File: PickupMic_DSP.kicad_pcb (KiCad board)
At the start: 4 copper layers, 70 x 59.8 mm, 46 parts, among them J201 Barrel_Jack, J301 Piezos, J401 USB_B_Micro, J402 SWD, U201 AMS1117-3.3, U202 AMS1117-5.0, U203 AMS1117-3.3, U301 TL082, U302 TL082, U303 ADS1115IDGS, U401 USBLC6-2SC6, U402 STM32F405RGTx, Y401 25Mhz

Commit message: Switch ADC
Switched from the ADS1115 to ADS7924 to get faster sampling time.
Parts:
- added C305: 1u, Capacitor_SMD:C_0402_1005Metric, F.Cu at (98.2, 93.8)
- added C306: 1u, Capacitor_SMD:C_0402_1005Metric, F.Cu at (98.2, 96.0)
- added D202: RED, LED_SMD:LED_0805_2012Metric, F.Cu at (100.0, 66.0)
- added D402: GREEN, LED_SMD:LED_0805_2012Metric, F.Cu at (103.4, 80.0)
- added kibuzzard-63BB1A01: G***, kibuzzard-63BB1A01, F.Cu at (124.2, 115.0)
- added kibuzzard-63BB1A56: G***, kibuzzard-63BB1A56, F.Cu at (124.2, 117.6)
- added kibuzzard-63BB1A7D: G***, kibuzzard-63BB1A7D, F.Cu at (124.4, 110.0)
- added kibuzzard-63BB1AB4: G***, kibuzzard-63BB1AB4, F.Cu at (135.0, 107.0)
- added kibuzzard-63BB1BAF: G***, kibuzzard-63BB1BAF, F.Cu at (100.2, 71.5)
- added kibuzzard-63C77ADE: G***, kibuzzard-63C77ADE, F.Cu at (77.8, 66.8)
- added kibuzzard-63C77B3E: G***, kibuzzard-63C77B3E, F.Cu at (101.4, 77.6)
- added kibuzzard-63CD6EAA: G***, kibuzzard-63CD6EAA, F.Cu at (124.2, 112.6)
- D201: value RED -> SS54; footprint LED_SMD:LED_0805_2012Metric -> Diode_SMD:D_SMA
- D401: value GREEN -> SS54; footprint LED_SMD:LED_0805_2012Metric -> Diode_SMD:D_SMA
- U303: value ADS1115IDGS -> ADS7924; footprint Package_SO:TSSOP-10_3x3mm_P0.5mm -> Package_DFN_QFN:WQFN-16-1EP_3x3mm_P0.5mm_EP1.68x1.68mm
- moved R308 21.4 mm to (84.3, 104.7), turned to 90 degrees
- moved R305 21.2 mm to (105.7, 106.0), turned to 90 degrees
- moved D201 12.4 mm to (90.2, 74.6), turned to 180 degrees
- moved U302 12.2 mm to (88.8, 105.8), turned to 180 degrees
- moved U301 12.1 mm to (101.1, 105.8), turned to 180 degrees
- moved C301 7.63 mm to (131.8, 110.0)
- moved R301 7.63 mm to (128.4, 110.0)
- moved C304 7.60 mm to (131.8, 117.6)
- moved R304 7.60 mm to (128.5, 117.6)
- moved D401 5.69 mm to (102.8, 74.4)
- moved R306 3.71 mm to (96.5, 104.7), turned to 90 degrees
- moved R307 3.08 mm to (93.4, 106.0), turned to 90 degrees
- moved C303 2.55 mm to (131.8, 115.1)
- moved R303 2.55 mm to (128.5, 115.1)
- moved C302 2.49 mm to (131.8, 112.5)
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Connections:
- C201 pad 2: +12V -> Vin
- C202 pad 2: +12V -> Vin
- D201 pad 1: Net-(D201-Pad1) -> Vin
- D201 pad 2: +3.3V -> Net-(D201-Pad2)
- D401 pad 1: Net-(D401-Pad1) -> Vin
- D401 pad 2: /Microcontroller/MCU_LED -> VBUS
- J201 pad 1: +12V -> Net-(D201-Pad2)
- J301 pad 2: /Analog In/AIN3 -> /Analog In/AIN0
- J301 pad 4: /Analog In/AIN2 -> /Analog In/AIN1
- J301 pad 6: /Analog In/AIN1 -> /Analog In/AIN2
- J301 pad 8: /Analog In/AIN0 -> /Analog In/AIN3
- R201 pad 1: Net-(D201-Pad1) -> Net-(D202-Pad1)
- R401 pad 1: Net-(D401-Pad1) -> Net-(D402-Pad1)
- U201 pad 3: +12V -> Vin
- U202 pad 3: +12V -> Vin
- U303 pad 1: GND -> unconnected-(U303-Pad1)
- U303 pad 10: /Analog In/MCU_SCL -> /Analog In/ADC_AIN2
- U303 pad 3: GND -> /Analog In/MCU_SCL
- U303 pad 4: /Analog In/ADC_AIN0 -> /Analog In/MCU_SDA
- U303 pad 5: /Analog In/ADC_AIN1 -> GND
- U303 pad 6: /Analog In/ADC_AIN2 -> GND
- U303 pad 7: /Analog In/ADC_AIN3 -> unconnected-(U303-Pad7)
- U303 pad 8: +5VA -> GND
- U303 pad 9: /Analog In/MCU_SDA -> /Analog In/ADC_AIN3
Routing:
- net Vin: track 0.00 -> 42.0 mm
- net /Analog In/FILT_AIN3: track 24.9 -> 60.4 mm
- net +12V: track 33.0 -> 0.00 mm
- net /Analog In/FILT_AIN0: track 53.8 -> 26.1 mm
- net VBUS: track 6.97 -> 21.7 mm, vias 0 -> 2
- net +3.3V: track 36.8 -> 28.1 mm, vias 16 -> 41
- net +5VA: track 59.8 -> 67.3 mm
- net /Analog In/ADC_AIN2: track 9.26 -> 15.0 mm
- net /Analog In/FILT_AIN2: track 39.2 -> 44.9 mm
- net Net-(D201-Pad2): track 0.00 -> 4.79 mm
- net GND: track 132.4 -> 128.7 mm, vias 53 -> 69
- net /Analog In/MCU_SDA: track 17.7 -> 21.0 mm, vias 0 -> 2
- net Net-(D202-Pad1): track 0.00 -> 3.19 mm
- net MCU_ADC_INT: track 22.5 -> 19.6 mm
- net /Analog In/ADC_AIN0: track 12.7 -> 15.2 mm
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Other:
- board text removed: "AIN0"
- board text removed: "AIN1"
- board text removed: "AIN2"
- board text removed: "AIN3"
- board text removed: "Blinky!"
- board text removed: "GND"
- board text removed: "Power"
- board text removed: "VIN: 9-12V DC"

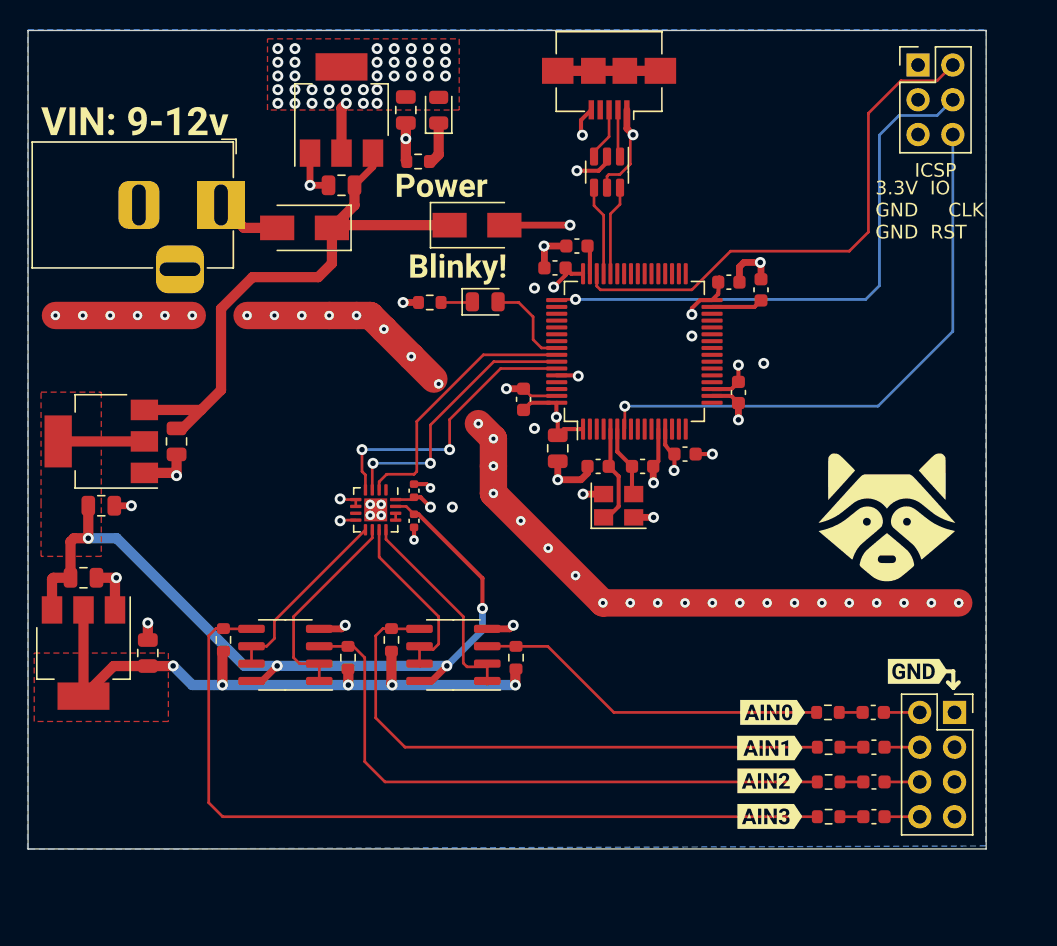
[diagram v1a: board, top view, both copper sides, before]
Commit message: Improvements
Switched ADC to ADC128S.
Upgraded USB to USB-C
Improved Analog front end to work with signals better.
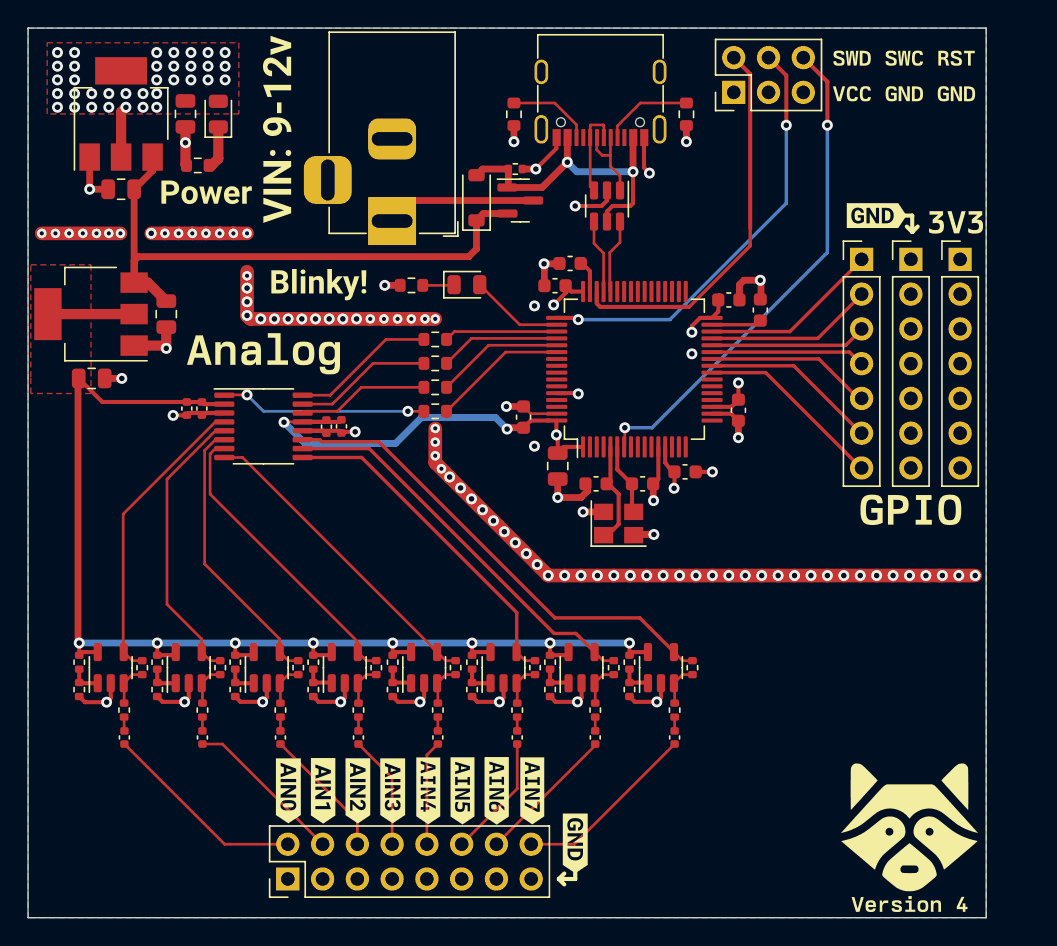
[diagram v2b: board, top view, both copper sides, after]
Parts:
- removed C205, C206: 22u, Capacitor_SMD:C_0805_2012Metric
- removed D401: SS54, Diode_SMD:D_SMA
- removed J402: SWD, Connector_PinHeader_2.54mm:PinHeader_2x03_P2.54mm_Vertical
- removed U203: AMS1117-3.3, Package_TO_SOT_SMD:SOT-223-3_TabPin2
- added C307: 1u, Capacitor_SMD:C_0402_1005Metric, F.Cu at (105.7, 111.8)
- added C308: 1u, Capacitor_SMD:C_0402_1005Metric, F.Cu at (99.9, 111.8)
- added C309: 1u, Capacitor_SMD:C_0402_1005Metric, F.Cu at (81.6, 87.8)
- added C310: 1u, Capacitor_SMD:C_0402_1005Metric, F.Cu at (92.9, 89.1)
- added C311: 100n, Capacitor_SMD:C_0402_1005Metric, F.Cu at (91.8, 89.1)
- added C312: 100n, Capacitor_SMD:C_0402_1005Metric, F.Cu at (82.7, 87.8)
- added J501: GPIO, Connector_PinHeader_2.54mm:PinHeader_1x07_P2.54mm_Vertical, F.Cu at (130.9, 76.9)
- added J502: VCC, Connector_PinHeader_2.54mm:PinHeader_1x07_P2.54mm_Vertical, F.Cu at (138.1, 76.9)
- added J503: GND, Connector_PinHeader_2.54mm:PinHeader_1x07_P2.54mm_Vertical, F.Cu at (134.5, 76.9)
- added J504: SWD, Connector_PinHeader_2.54mm:PinHeader_2x03_P2.54mm_Vertical, F.Cu at (121.6, 64.7)
- added Q201: AO3401A, Package_TO_SOT_SMD:SOT-23, F.Cu at (106.0, 72.6)
- added R202: 100k, Resistor_SMD:R_0402_1005Metric, F.Cu at (105.6, 70.3)
- added R309: 510R, Resistor_SMD:R_0402_1005Metric, F.Cu at (94.1, 109.8)
- added R310: 510R, Resistor_SMD:R_0402_1005Metric, F.Cu at (88.4, 109.8)
- added R311: 510R, Resistor_SMD:R_0402_1005Metric, F.Cu at (82.7, 109.8)
- added R312: 510R, Resistor_SMD:R_0402_1005Metric, F.Cu at (77.0, 109.8)
- added R313: 100k, Resistor_SMD:R_0402_1005Metric, F.Cu at (95.4, 106.7)
- added R314: 100k, Resistor_SMD:R_0402_1005Metric, F.Cu at (89.7, 106.7)
- added R315: 100k, Resistor_SMD:R_0402_1005Metric, F.Cu at (84.0, 106.7)
- added R316: 100k, Resistor_SMD:R_0402_1005Metric, F.Cu at (78.3, 106.7)
- added R317: 10k, Resistor_SMD:R_0402_1005Metric, F.Cu at (113.9, 106.3)
- added R318: 10k, Resistor_SMD:R_0402_1005Metric, F.Cu at (113.9, 108.3)
- added R319: 10k, Resistor_SMD:R_0402_1005Metric, F.Cu at (108.1, 106.3)
- added R320: 10k, Resistor_SMD:R_0402_1005Metric, F.Cu at (108.1, 108.3)
- added R321: 10k, Resistor_SMD:R_0402_1005Metric, F.Cu at (102.4, 106.3)
- added R322: 10k, Resistor_SMD:R_0402_1005Metric, F.Cu at (102.4, 108.3)
- added R323: 10k, Resistor_SMD:R_0402_1005Metric, F.Cu at (96.6, 106.3)
- added R324: 10k, Resistor_SMD:R_0402_1005Metric, F.Cu at (96.6, 108.3)
- added R325: 510R, Resistor_SMD:R_0402_1005Metric, F.Cu at (117.2, 109.8)
- added R326: 510R, Resistor_SMD:R_0402_1005Metric, F.Cu at (111.4, 109.8)
- added R327: 510R, Resistor_SMD:R_0402_1005Metric, F.Cu at (105.7, 109.8)
- added R328: 510R, Resistor_SMD:R_0402_1005Metric, F.Cu at (99.9, 109.8)
- added R329: 100k, Resistor_SMD:R_0402_1005Metric, F.Cu at (118.5, 106.7)
- added R330: 100k, Resistor_SMD:R_0402_1005Metric, F.Cu at (112.8, 106.7)
- added R331: 100k, Resistor_SMD:R_0402_1005Metric, F.Cu at (107.0, 106.7)
- added R332: 100k, Resistor_SMD:R_0402_1005Metric, F.Cu at (101.2, 106.7)
- added R402: 5.1k, Resistor_SMD:R_0603_1608Metric, F.Cu at (118.1, 66.3)
- added R403: 5.1k, Resistor_SMD:R_0603_1608Metric, F.Cu at (105.5, 66.3)
- added R404: 100, Resistor_SMD:R_0603_1608Metric, F.Cu at (99.8, 82.8)
- added R405: 100, Resistor_SMD:R_0603_1608Metric, F.Cu at (99.8, 84.5)
- added R406: 100, Resistor_SMD:R_0603_1608Metric, F.Cu at (99.8, 86.2)
- added R407: 100, Resistor_SMD:R_0603_1608Metric, F.Cu at (99.8, 88.0)
- added U304: LMV321, Package_TO_SOT_SMD:SOT-23-5, F.Cu at (76.0, 106.7)
- added U305: LMV321, Package_TO_SOT_SMD:SOT-23-5, F.Cu at (116.2, 106.7)
- added U306: LMV321, Package_TO_SOT_SMD:SOT-23-5, F.Cu at (110.4, 106.7)
- added U307: LMV321, Package_TO_SOT_SMD:SOT-23-5, F.Cu at (104.7, 106.7)
- added U308: LMV321, Package_TO_SOT_SMD:SOT-23-5, F.Cu at (98.9, 106.7)
- added U309: ADC128S102, Package_SO:TSSOP-16_4.4x5mm_P0.65mm, F.Cu at (87.2, 89.1)
- added kibuzzard-63BB1AB4: G***, kibuzzard-63BB1AB4, F.Cu at (132.0, 73.7)
- added kibuzzard-641D0A5C: G***, kibuzzard-641D0A5C, F.Cu at (101.7, 115.7)
- added kibuzzard-641D0A72: G***, kibuzzard-641D0A72, F.Cu at (104.2, 115.7)
- added kibuzzard-641D0A85: G***, kibuzzard-641D0A85, F.Cu at (106.8, 115.7)
- added kibuzzard-641E03D9: G***, kibuzzard-641E03D9, F.Cu at (99.2, 115.7)
- added kibuzzard-6422FB8B: G***, kibuzzard-6422FB8B, F.Cu at (137.8, 74.2)
- added kibuzzard-6422FF5E: G***, kibuzzard-6422FF5E, F.Cu at (134.4, 124.0)
- added kibuzzard-642304B8: G***, kibuzzard-642304B8, F.Cu at (134.5, 95.2)
- added kibuzzard-6423A336: G***, kibuzzard-6423A336, F.Cu at (87.2, 83.8)
- added kibuzzard-6423A404: G***, kibuzzard-6423A404, F.Cu at (134.0, 64.8)
- added kibuzzard-6423A41B: G***, kibuzzard-6423A41B, F.Cu at (134.0, 62.2)
- C301, C302, C303, C304: value 10u -> 1u; footprint Capacitor_SMD:C_0603_1608Metric -> Capacitor_SMD:C_0402_1005Metric
- C401: value 30p -> 2.2u
- C404: value 2.2u -> 30p
- D201: value SS54 -> MBR120; footprint Diode_SMD:D_SMA -> Diode_SMD:D_SOD-123
- J301: value Piezos -> AIN; footprint Connector_PinSocket_2.54mm:PinSocket_2x04_P2.54mm_Vertical -> Connector_PinHeader_2.54mm:PinHeader_2x08_P2.54mm_Vertical
- J401: value USB_B_Micro -> USB_C_Receptacle_USB2.0; footprint Connector_USB:USB_Micro-B_Amphenol_10104110_Horizontal -> Connector_USB:USB_C_Receptacle_G-Switch_GT-USB-7010ASV
- R301, R302, R303, R304, R305, R306, R307, R308: footprint Resistor_SMD:R_0603_1608Metric -> Resistor_SMD:R_0402_1005Metric
- U301, U302: value TL082 -> LMV321; footprint Package_SO:SOIC-8_3.9x4.9mm_P1.27mm -> Package_TO_SOT_SMD:SOT-23-5
- U303: value ADS7924 -> LMV321; footprint Package_DFN_QFN:WQFN-16-1EP_3x3mm_P0.5mm_EP1.68x1.68mm -> Package_TO_SOT_SMD:SOT-23-5
- Y401: value 25Mhz -> 16Mhz
- moved C304 55.1 mm to (77.0, 111.8), turned to 90 degrees
- moved J301 50.2 mm to (89.0, 122.2), turned to 90 degrees
- moved C303 49.2 mm to (82.7, 111.8), turned to 90 degrees
- moved R304 44.3 mm to (85.1, 108.3), turned to -90 degrees
- moved R303 44.2 mm to (85.1, 106.3), turned to -90 degrees
- moved C302 43.4 mm to (88.4, 111.8), turned to 90 degrees
- moved R302 37.9 mm to (90.8, 108.3), turned to 90 degrees
- moved R301 37.8 mm to (90.8, 106.3), turned to -90 degrees
- moved C301 37.7 mm to (94.1, 111.8), turned to 90 degrees
- moved kibuzzard-63BB1A7D 35.8 mm to (89.0, 115.7), turned to -90 degrees
- moved kibuzzard-63CD6EAA 32.8 mm to (91.6, 115.7), turned to -90 degrees
- moved kibuzzard-63BB1A01 30.1 mm to (94.1, 115.7), turned to -90 degrees
- moved kibuzzard-63BB1AB4 28.0 mm to (110.0, 119.6), turned to -90 degrees
- moved kibuzzard-63BB1A56 27.6 mm to (96.6, 115.7), turned to -90 degrees
- moved C305 26.2 mm to (117.2, 111.8)
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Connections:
- C201 pad 2: Vin -> +5V
- C202 pad 2: Vin -> +5V
- C301 pad 1: /Analog In/AIN0 -> /Analog In/AIN3
- C302 pad 1: /Analog In/AIN1 -> /Analog In/AIN2
- C303 pad 1: /Analog In/AIN2 -> /Analog In/AIN1
- C304 pad 1: /Analog In/AIN3 -> /Analog In/AIN0
- C305 pad 1: +3.3V -> /Analog In/AIN7
- C305 pad 2: GND -> Net-(C305-Pad2)
- C306 pad 1: +5VA -> /Analog In/AIN6
- C306 pad 2: GND -> Net-(C306-Pad2)
- C401 pad 1: /Microcontroller/MCU_PH0 -> /Microcontroller/MCU_VCAP1
- C402 pad 1: /Microcontroller/MCU_PH1 -> /Microcontroller/MCU_PH0
- C403 pad 1: /Microcontroller/MCU_VCAP1 -> /Microcontroller/MCU_VCAP2
- C404 pad 1: /Microcontroller/MCU_VCAP2 -> /Microcontroller/MCU_PH1
- D201 pad 1: Vin -> +5V
- D201 pad 2: Net-(D201-Pad2) -> VBUS
- J201 pad 1: Net-(D201-Pad2) -> Vin
- R301 pad 1: Net-(C301-Pad2) -> +5VA
- R301 pad 2: /Analog In/FILT_AIN0 -> Net-(U301-+)
- R302 pad 1: Net-(C302-Pad2) -> GND
- R302 pad 2: /Analog In/FILT_AIN1 -> Net-(U301-+)
- R303 pad 1: Net-(C303-Pad2) -> +5VA
- R303 pad 2: /Analog In/FILT_AIN2 -> Net-(U302-+)
- R304 pad 1: Net-(C304-Pad2) -> Net-(U302-+)
- R304 pad 2: /Analog In/FILT_AIN3 -> GND
- R305 pad 1: +3.3VA -> +5VA
- R305 pad 2: /Analog In/FILT_AIN0 -> Net-(U303-+)
- R306 pad 1: +3.3VA -> GND
- R306 pad 2: /Analog In/FILT_AIN1 -> Net-(U303-+)
- R307 pad 1: +3.3VA -> +5VA
- R307 pad 2: /Analog In/FILT_AIN2 -> Net-(U304-+)
- R308 pad 1: +3.3VA -> GND
- R308 pad 2: /Analog In/FILT_AIN3 -> Net-(U304-+)
- U201 pad 3: Vin -> +5V
- U202 pad 3: Vin -> +5V
- U301 pad 1: /Analog In/ADC_AIN0 -> Net-(U301-+)
- U301 pad 2: /Analog In/ADC_AIN0 -> GND
- U301 pad 3: /Analog In/FILT_AIN0 -> Net-(U301--)
- U301 pad 4: GND -> /Analog In/ADC_AIN3
- U301 pad 5: /Analog In/FILT_AIN1 -> +5VA
- U302 pad 1: /Analog In/ADC_AIN2 -> Net-(U302-+)
- U302 pad 2: /Analog In/ADC_AIN2 -> GND
- U302 pad 3: /Analog In/FILT_AIN2 -> Net-(U302--)
- U302 pad 4: GND -> /Analog In/ADC_AIN2
- U302 pad 5: /Analog In/FILT_AIN3 -> +5VA
- U303 pad 1: unconnected-(U303-Pad1) -> Net-(U303-+)
- U303 pad 2: MCU_ADC_INT -> GND
- U303 pad 3: /Analog In/MCU_SCL -> Net-(U303--)
- U303 pad 4: /Analog In/MCU_SDA -> /Analog In/ADC_AIN1
- U303 pad 5: GND -> +5VA
- U402 pad 24: unconnected-(U402-Pad24) -> MCU_GPIO_PC04
- U402 pad 25: unconnected-(U402-Pad25) -> MCU_GPIO_PC05
- U402 pad 26: unconnected-(U402-Pad26) -> MCU_GPIO_PB00
- U402 pad 27: unconnected-(U402-Pad27) -> MCU_GPIO_PB01
- U402 pad 28: unconnected-(U402-Pad28) -> MCU_GPIO_PB02
- U402 pad 29: unconnected-(U402-Pad29) -> MCU_GPIO_PB10
- U402 pad 30: unconnected-(U402-Pad30) -> MCU_GPIO_PB11
- U402 pad 46: /Microcontroller/MCU_SWD_IO -> MCU_SWD_IO
- U402 pad 49: /Microcontroller/MCU_SWD_CLK -> MCU_SWD_CLK
- U402 pad 50: unconnected-(U402-Pad50) -> /Microcontroller/MCU_LED
- U402 pad 51: unconnected-(U402-Pad51) -> Net-(U402-PC10)
- U402 pad 52: unconnected-(U402-Pad52) -> Net-(U402-PC11)
- U402 pad 53: unconnected-(U402-Pad53) -> Net-(U402-PC12)
- U402 pad 54: unconnected-(U402-Pad54) -> Net-(U402-PD2)
- U402 pad 56: /Microcontroller/MCU_LED -> unconnected-(U402-PB4-Pad56)
- U402 pad 57: MCU_ADC_INT -> unconnected-(U402-PB5-Pad57)
- U402 pad 58: /Analog In/MCU_SCL -> unconnected-(U402-PB6-Pad58)
- U402 pad 59: /Analog In/MCU_SDA -> unconnected-(U402-PB7-Pad59)
- U402 pad 7: /Microcontroller/MCU_NRST -> MCU_NRST
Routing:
- net /Analog In/FILT_AIN3: track 60.4 -> 0.00 mm
- net +3.3VA: track 46.5 -> 0.00 mm, vias 5 -> 0
- net /Analog In/FILT_AIN2: track 44.9 -> 0.00 mm
- net +5V: track 0.00 -> 44.2 mm
- net /Analog In/FILT_AIN1: track 42.6 -> 0.00 mm
- net /Microcontroller/MCU_NRST: track 42.3 -> 0.00 mm, vias 1 -> 0
- net /Microcontroller/MCU_SWD_CLK: track 41.4 -> 0.00 mm, vias 1 -> 0
- net GND: track 128.7 -> 168.3 mm, vias 69 -> 106
- net /Microcontroller/MCU_SWD_IO: track 38.9 -> 0.00 mm
- net MCU_NRST: track 0.00 -> 36.4 mm, vias 0 -> 2
- net /Analog In/ADC_AIN7: track 0.00 -> 35.2 mm
- net Vin: track 42.0 -> 8.80 mm
- net MCU_SWD_CLK: track 0.00 -> 31.5 mm, vias 0 -> 2
- net /Analog In/ADC_AIN6: track 0.00 -> 29.1 mm
- net +5VA: track 67.3 -> 96.1 mm, vias 4 -> 8
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- removed copper zone on F.Cu, net +3.3VA
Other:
- board size 70 x 59.8 mm -> 70 x 65 mm
- board text removed: "3.3V IO GND CLK GND RST"
- board text removed: "ICSP"
